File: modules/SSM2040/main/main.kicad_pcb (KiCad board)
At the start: 2 copper layers, 40.3 x 111.8 mm, 59 parts, among them IC1 RC4136, J1 IDC Header, J2 Conn_01x07_Female, Q1 2N3906, U1 LM741, U2 SSM2040, U3 CA3080

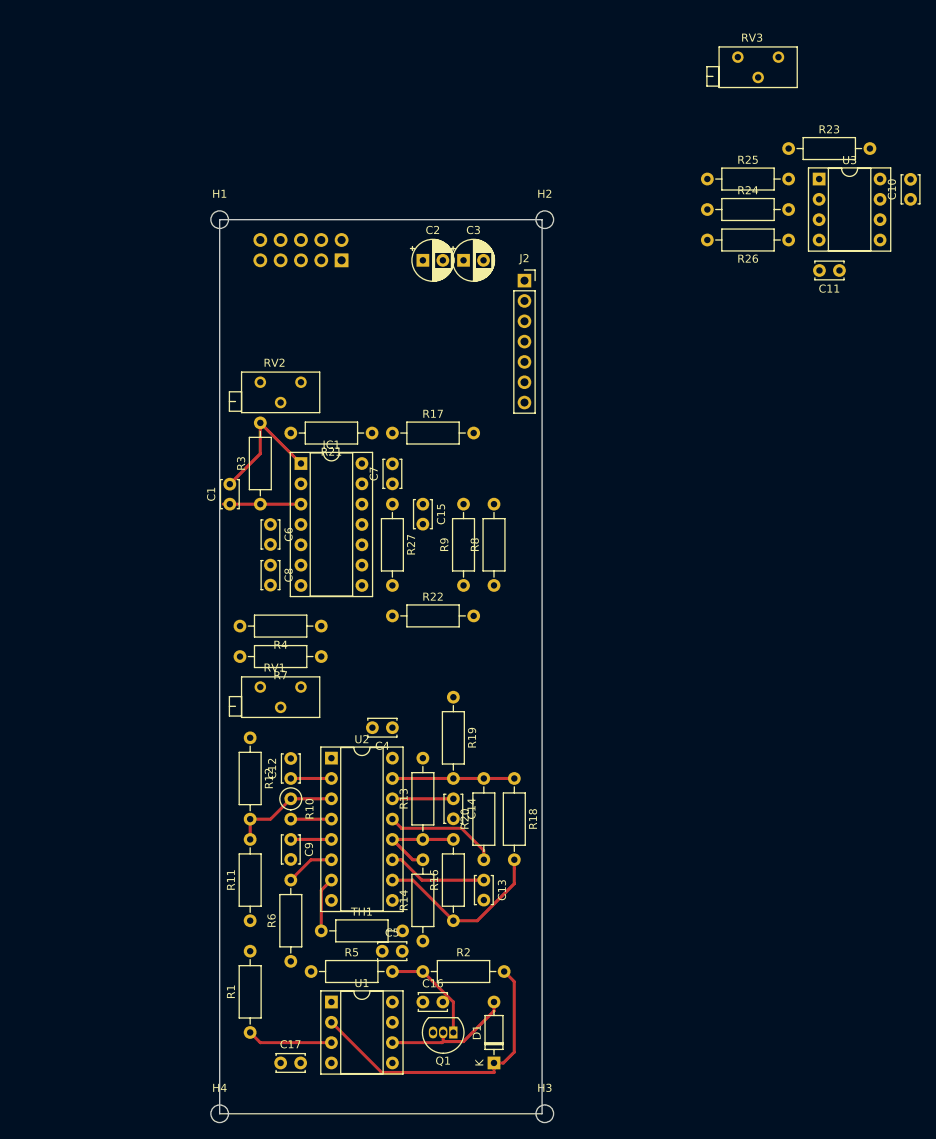
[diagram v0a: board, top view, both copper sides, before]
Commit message: update power supply
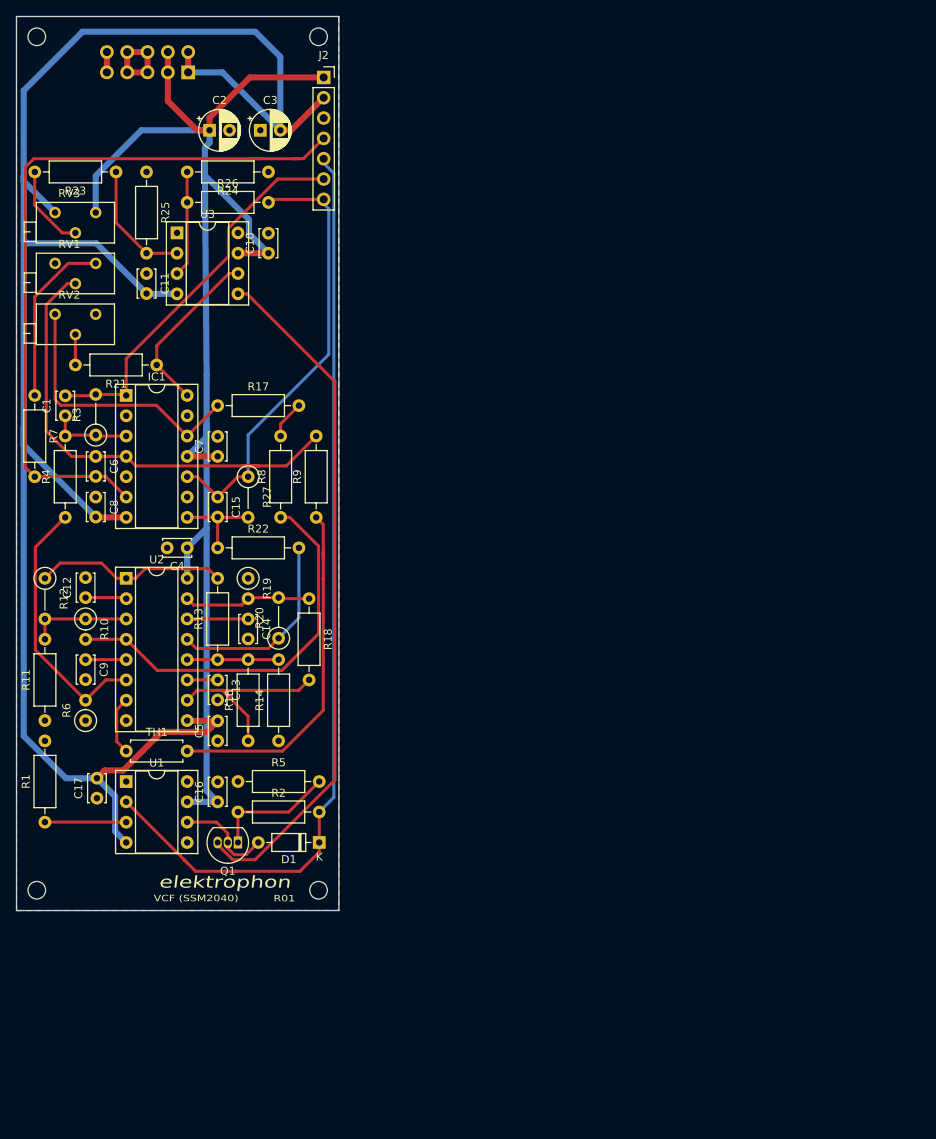
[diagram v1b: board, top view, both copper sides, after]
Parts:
- added REF**: elektrophon logo, elektrophon:elektrophon logo, F.Cu at (51.4, 134.6)
- R12, R20, R27, R3: footprint Resistor_THT:R_Axial_DIN0207_L6.3mm_D2.5mm_P10.16mm_Horizontal -> Resistor_THT:R_Axial_DIN0207_L6.3mm_D2.5mm_P5.08mm_Vertical
- R19, R6: footprint Resistor_THT:R_Axial_DIN0207_L6.3mm_D2.5mm_P10.16mm_Horizontal -> Resistor_THT:R_Axial_DIN0207_L6.3mm_D2.5mm_P2.54mm_Vertical
- TH1: footprint Resistor_THT:R_Axial_DIN0207_L6.3mm_D2.5mm_P10.16mm_Horizontal -> Resistor_THT:R_Axial_DIN0207_L6.3mm_D2.5mm_P7.62mm_Horizontal
- moved RV3 87.5 mm to (35.3, 49.9)
- moved C11 86.6 mm to (41.7, 57.5), turned to 270 degrees
- moved R23 84.1 mm to (37.8, 44.8), turned to 180 degrees
- moved U3 80.5 mm to (45.5, 52.5)
- moved C10 80.5 mm to (56.9, 55.0)
- moved R26 75.3 mm to (46.7, 48.6), turned to 0 degrees
- moved R25 70.1 mm to (41.7, 44.8), turned to 270 degrees
- moved RV1 58.8 mm to (35.3, 56.3)
- moved R24 55.1 mm to (56.9, 44.8), turned to 180 degrees
- moved R7 48.5 mm to (27.7, 72.8), turned to 270 degrees
- moved C13 41.6 mm to (50.5, 108.3)
- moved C17 40.3 mm to (35.5, 123.1), turned to 90 degrees
- moved H3 39.8 mm to (63.2, 134.6)
- moved R6 39.5 mm to (34.0, 113.4)
- moved R20 37.7 mm to (58.2, 103.1)
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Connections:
- J2 pad 1: /VC -> +15V
- J2 pad 2: /RES -> -15V
- J2 pad 3: /IN -> GND
- J2 pad 4: /OUT -> /VC
- J2 pad 5: +15V -> /RES
- J2 pad 6: -15V -> /IN
- J2 pad 7: GND -> /OUT
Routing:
- net -15V: track 0.00 -> 240.2 mm
- net +15V: track 0.00 -> 173.3 mm
- net /VC: track 0.00 -> 92.5 mm
- net /BIAS: track 0.00 -> 86.3 mm
- net /RES: track 37.8 -> 118.0 mm
- net Net-(C6-Pad1): track 0.00 -> 59.4 mm
- net /OUT: track 0.00 -> 56.1 mm
- net Net-(R10-Pad2): track 5.08 -> 49.8 mm
- net /CNTL: track 0.00 -> 44.6 mm
- net Net-(IC1-Pad12): track 0.00 -> 34.5 mm
- net /IN: track 16.4 -> 48.4 mm
- net Net-(R4-Pad1): track 6.13 -> 33.1 mm
- net Net-(R12-Pad1): track 0.00 -> 24.2 mm
- net Net-(IC1-Pad14): track 0.00 -> 21.7 mm
- net Net-(R7-Pad1): track 0.00 -> 21.7 mm
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- added copper zone on B.Cu, net GND

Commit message: update schematic
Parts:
- C12, C13, C14, C9: footprint Capacitor_THT:C_Disc_D3.4mm_W2.1mm_P2.50mm -> Capacitor_THT:C_Rect_L7.2mm_W5.5mm_P5.00mm_FKS2_FKP2_MKS2_MKP2
- R13, R14, R18: footprint Resistor_THT:R_Axial_DIN0207_L6.3mm_D2.5mm_P10.16mm_Horizontal -> Resistor_THT:R_Axial_DIN0207_L6.3mm_D2.5mm_P2.54mm_Vertical
- R16: footprint Resistor_THT:R_Axial_DIN0207_L6.3mm_D2.5mm_P10.16mm_Horizontal -> Resistor_THT:R_Axial_DIN0207_L6.3mm_D2.5mm_P5.08mm_Vertical
- moved R14 20.4 mm to (58.2, 95.5), turned to 270 degrees
- moved R19 13.6 mm to (50.5, 108.7), turned to 90 degrees
- moved R16 12.8 mm to (54.3, 103.2)
- moved R18 11.8 mm to (50.5, 101.3)
- moved C13 11.8 mm to (59.6, 100.8)
- moved C14 9.73 mm to (59.6, 108.9)
- moved R20 8.75 mm to (54.3, 110.9)
- moved R13 7.65 mm to (50.5, 98.1)
- moved R6 3.82 mm to (33.0, 117.1), turned to 0 degrees
- moved C9 2.57 mm to (34.1, 108.4)
- moved C12 0.86 mm to (34.0, 97.2)
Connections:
- R4 pad 1: Net-(R4-Pad1) -> Net-(R17-Pad2)
- R6 pad 2: Net-(R4-Pad1) -> Net-(R17-Pad2)
- TH1 pad 1: Net-(TH1-Pad1) -> GND
- U2 pad 10: Net-(R16-Pad1) -> Net-(R20-Pad1)
- U2 pad 11: Net-(C13-Pad1) -> Net-(C14-Pad1)
- U2 pad 12: Net-(R13-Pad1) -> Net-(R18-Pad1)
- U2 pad 13: Net-(R20-Pad1) -> Net-(R16-Pad1)
- U2 pad 14: Net-(C14-Pad1) -> Net-(C13-Pad1)
- U2 pad 15: Net-(R18-Pad1) -> Net-(R13-Pad1)
- U2 pad 6: Net-(R4-Pad1) -> Net-(R17-Pad2)
- U2 pad 7: Net-(TH1-Pad1) -> /CNTL
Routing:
- net Net-(R17-Pad2): track 4.76 -> 83.6 mm
- net Net-(R4-Pad1): track 33.1 -> 0.00 mm
- net Net-(R10-Pad2): track 49.8 -> 60.4 mm
- net Net-(R16-Pad1): track 24.7 -> 14.1 mm
- net /CNTL: track 44.6 -> 54.9 mm
- net Net-(C13-Pad1): track 3.81 -> 13.9 mm
- net Net-(R20-Pad1): track 24.8 -> 33.0 mm
- net Net-(TH1-Pad1): track 7.34 -> 0.00 mm
- net Net-(C14-Pad1): track 7.62 -> 13.9 mm
- net Net-(R18-Pad1): track 16.0 -> 13.8 mm
- net Net-(C6-Pad1): track 59.4 -> 57.6 mm
- net Net-(C9-Pad1): track 5.08 -> 6.04 mm
- net Net-(C12-Pad1): track 5.13 -> 5.67 mm

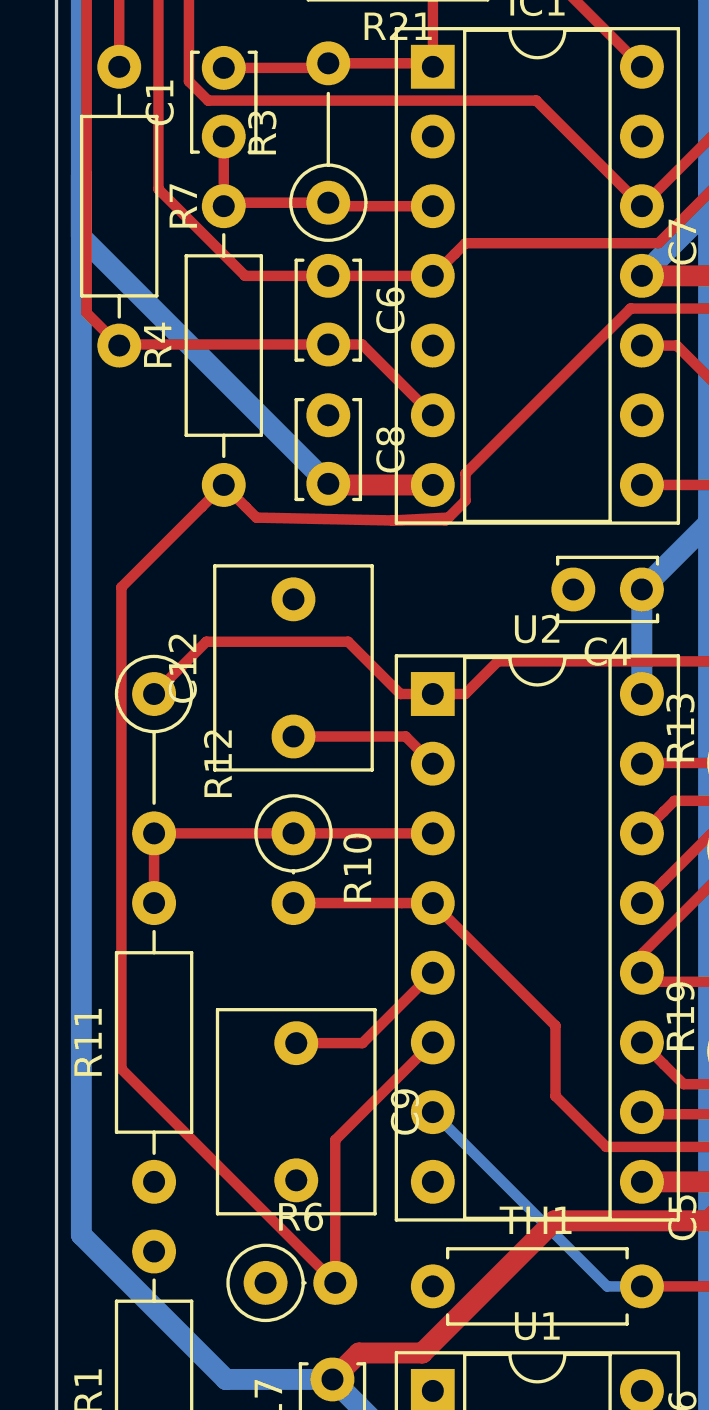
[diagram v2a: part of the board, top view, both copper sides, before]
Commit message: update schematic
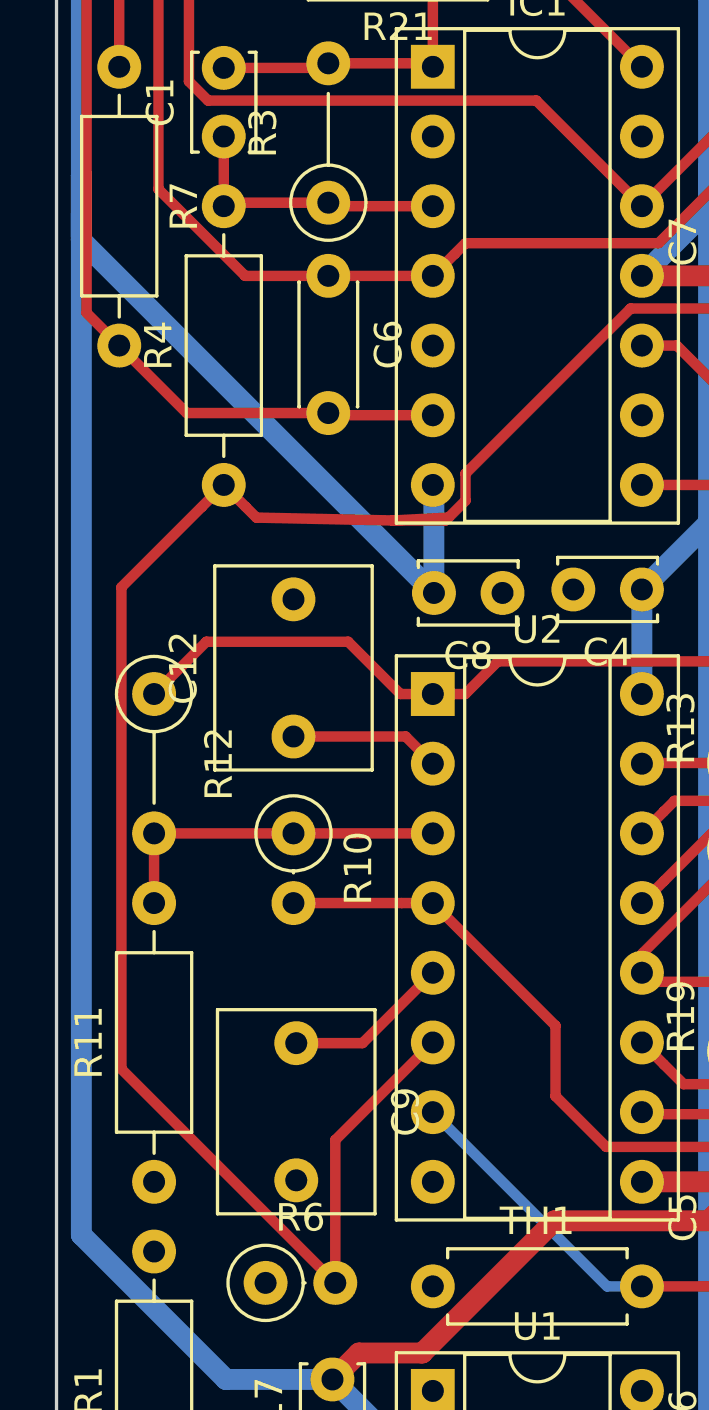
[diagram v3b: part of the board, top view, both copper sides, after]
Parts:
- C6: value C -> 0.05u; footprint Capacitor_THT:C_Disc_D3.4mm_W2.1mm_P2.50mm -> Capacitor_THT:C_Disc_D4.3mm_W1.9mm_P5.00mm
- moved C8 9.07 mm to (41.7, 91.9), turned to 180 degrees
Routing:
- net -15V: track 240.3 -> 246.8 mm
